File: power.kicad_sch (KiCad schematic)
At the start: 10 parts, among them P1 POWER, Q2 DMP3056L-7, U1 REG1117-3.3, U3 REG1117A-1.8

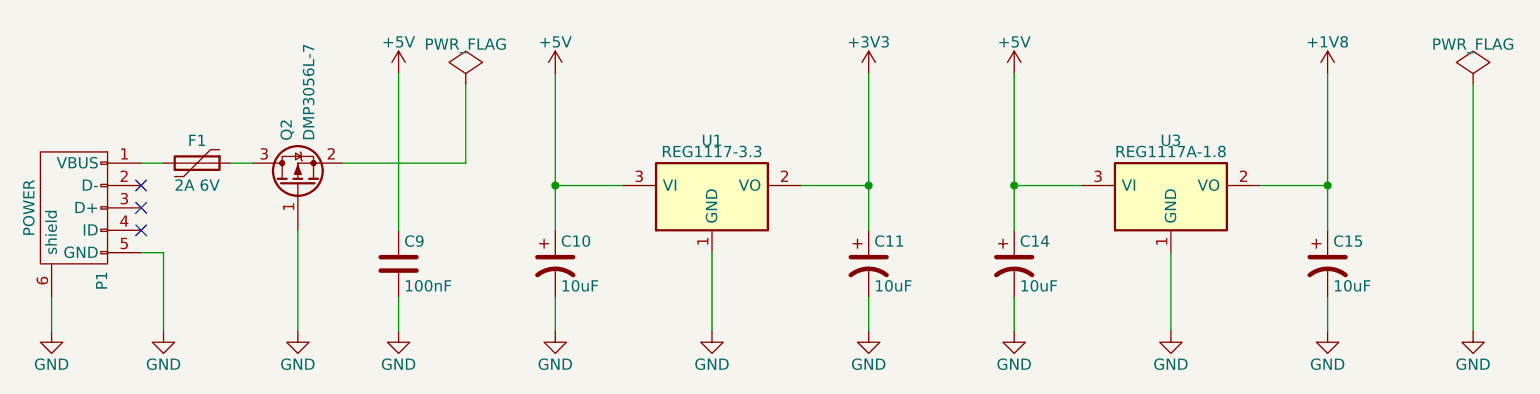
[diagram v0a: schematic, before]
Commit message: fix 5v erc connection
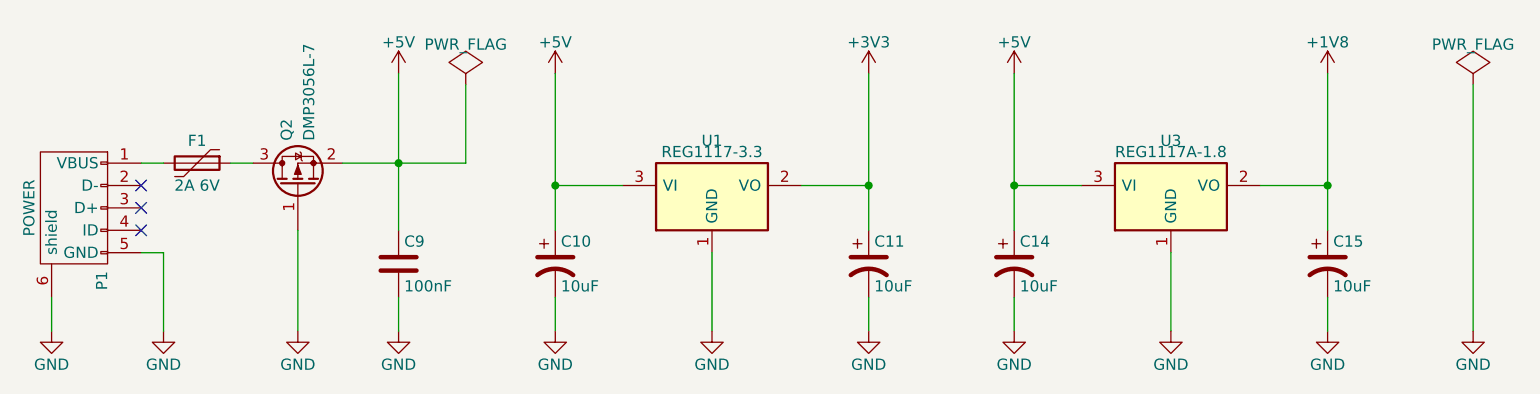
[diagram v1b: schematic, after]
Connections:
- net +5V: now also Q2.2 (S)
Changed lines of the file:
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@@
+	)
+	(junction
+		(at 66.04 34.29)
+		(diameter 0)
+		(color 0 0 0 0)
 	)
 	(junction
@@
 	(wire
 		(pts
-			(xy 59.69 34.29) (xy 73.66 34.29)
+			(xy 59.69 34.29) (xy 66.04 34.29)
 		)
 		(stroke
@@
 	(wire
 		(pts
+			(xy 66.04 34.29) (xy 73.66 34.29)
+		)
+		(stroke
+			(width 0)
+			(type default)
+		)
+	)
+	(wire
+		(pts
 			(xy 153.67 44.45) (xy 153.67 53.34)
 		)
@@
 	(wire
 		(pts
-			(xy 66.04 24.13) (xy 66.04 41.91)
-		)
-		(stroke
+			(xy 66.04 24.13) (xy 66.04 34.29)
+		)
+		(stroke
+			(width 0)
+			(type default)
+		)
+	)
+	(wire
+		(pts
+			(xy 66.04 34.29) (xy 66.04 41.91)
+		)
+		(stroke
